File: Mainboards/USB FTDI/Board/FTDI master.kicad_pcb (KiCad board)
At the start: 2 copper layers, 67.4 x 54.3 mm, 52 parts, among them IC1 NCP1117ST, IC10 FT232RL, IC2 MCP1700T-1802E, IC3 CRE1S0505SC, IC4 IL0512S, IC5 IRF7416, IC7 MAX14932, IC8 MAX14932, IC9 MAX14932, J1 USB_C_Receptacle_USB2.0, X2 AKL18X-04W, X3 IDC-Header_2x05_P2.54mm_Verti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, X4 ALLSERIALMASTERM

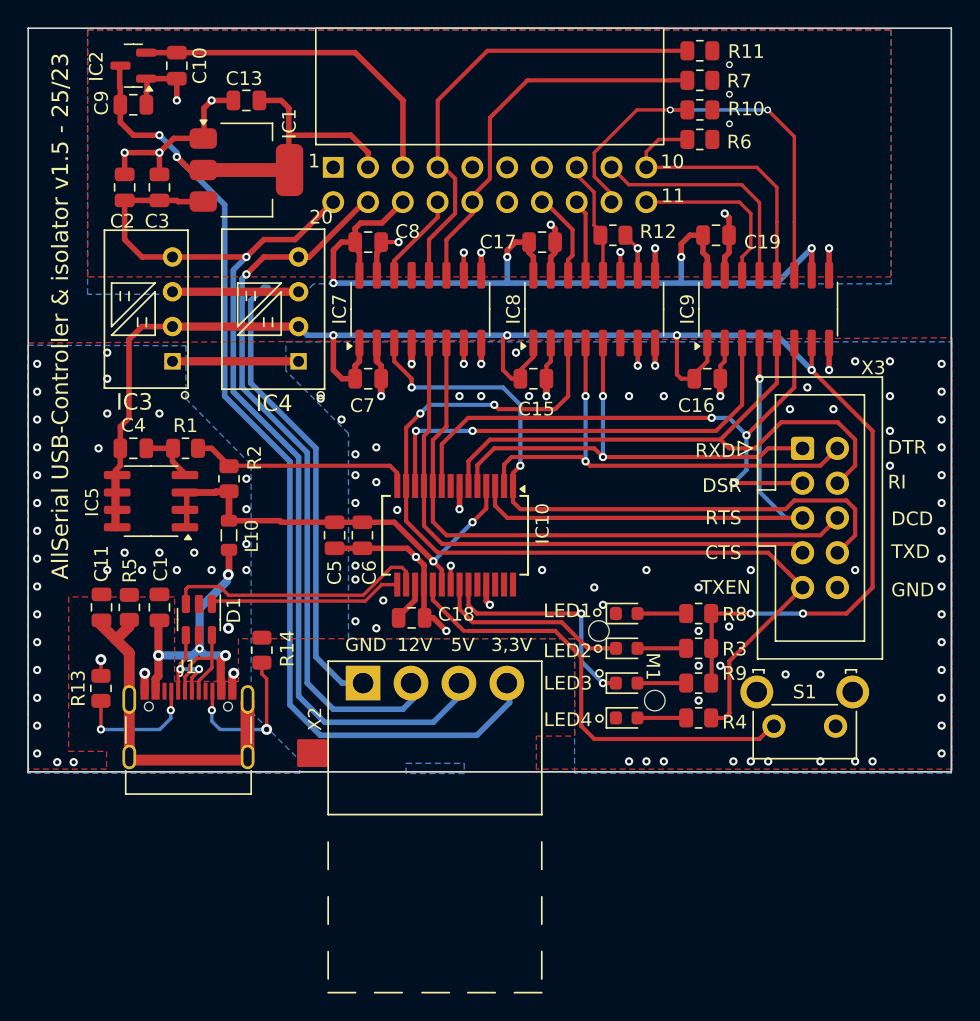
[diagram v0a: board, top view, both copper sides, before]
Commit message: Migrate to new KiCad Version
Add SMA connector front
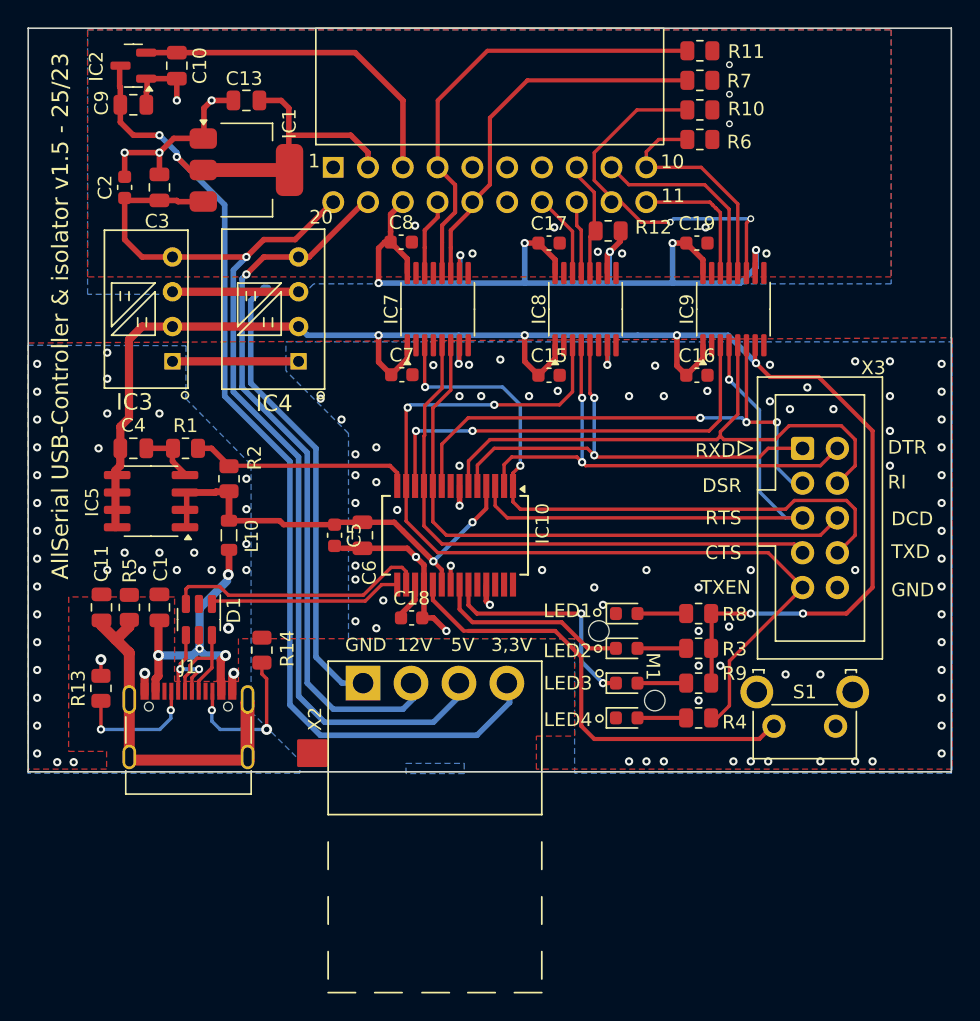
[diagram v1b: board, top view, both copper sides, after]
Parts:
- C15, C16, C17, C18, C19, C2, C5, C7, C8: footprint Capacitor_SMD:C_0805_2012Metric -> Capacitor_SMD:C_0603_1608Metric
- IC7, IC8, IC9: value MAX14932 -> ADuM142E0BRQZ-RL7; footprint Package_SO:SOIC-16_3.9x9.9mm_P1.27mm -> Package_SO:QSOP-16_3.9x4.9mm_P0.635mm
- L10: value WE-CBF_0805 -> ~
- moved IC9 2.54 mm to (166.3, 98.1)
- moved C7 2.48 mm to (142.1, 102.9)
- moved C8 2.41 mm to (142.0, 93.2)
- moved C19 1.51 mm to (163.6, 93.3)
- moved IC7 1.27 mm to (144.7, 98.1)
- moved C15 1.17 mm to (152.8, 102.9)
- moved C16 0.80 mm to (163.6, 102.9)
- moved IC8 0.64 mm to (155.5, 98.1)
- moved C17 0.51 mm to (152.8, 93.3)
- moved R12 0.47 mm to (157.1, 92.4)
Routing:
- net GND1: track 82.5 -> 62.9 mm
- net GND: track 48.2 -> 30.0 mm, vias 114 -> 115
- net Vio: track 74.1 -> 63.0 mm
- net Net-(IC9E-INB): track 32.1 -> 27.2 mm
- net +5V: track 131.6 -> 127.2 mm
- net Net-(IC10-~{DSR}): track 43.6 -> 39.7 mm
- net Net-(IC9D-INB): track 20.9 -> 17.3 mm
- net Net-(IC9C-OUTB): track 17.1 -> 14.5 mm
- net Net-(IC9B-OUTB): track 12.6 -> 10.1 mm
- net Net-(IC10-~{RI}): track 44.6 -> 42.6 mm
- net Net-(IC10-TXD): track 48.8 -> 47.3 mm
- net Net-(IC7B-OUTB): track 6.97 -> 6.01 mm
- net Net-(IC10-CBUS4): track 33.0 -> 32.1 mm
- net Net-(IC10-~{RTS}): track 39.0 -> 39.9 mm

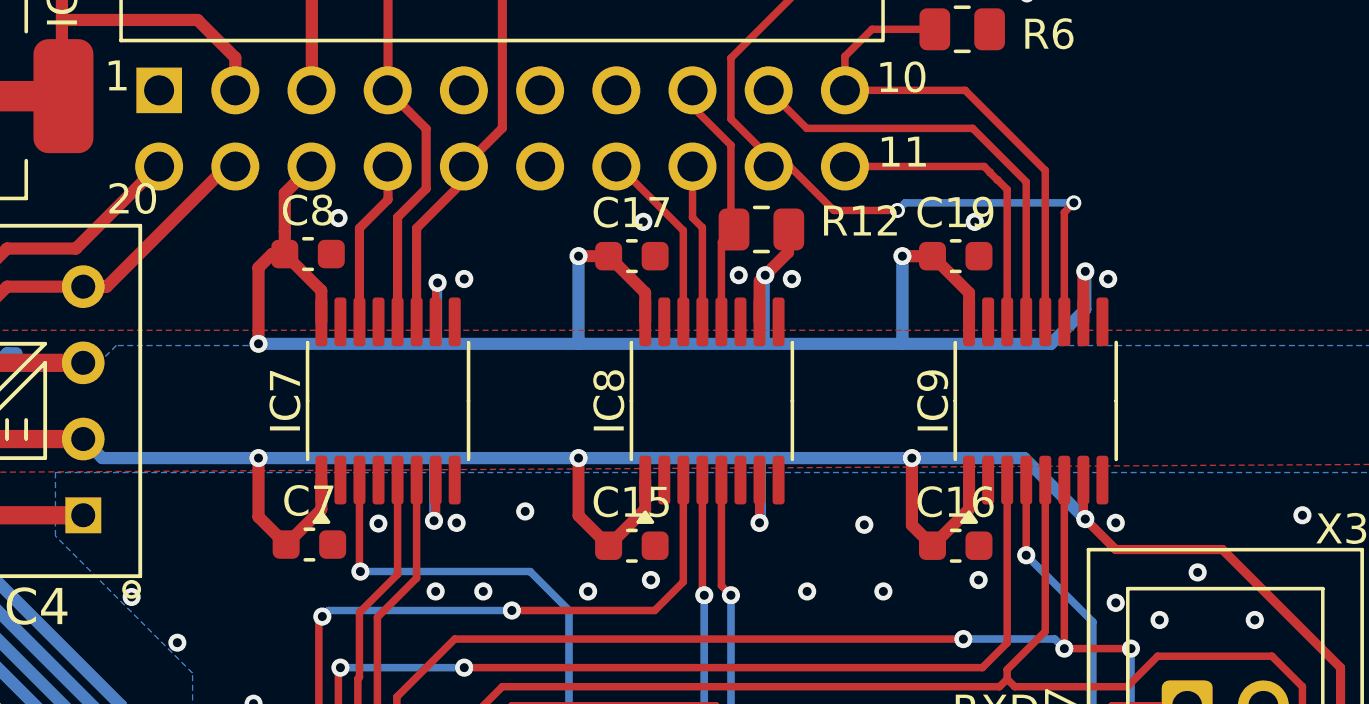
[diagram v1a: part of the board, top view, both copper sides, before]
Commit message: Update TTY CL slave board
Add ESP32 S3 WiFi MasterBoard
Update libs
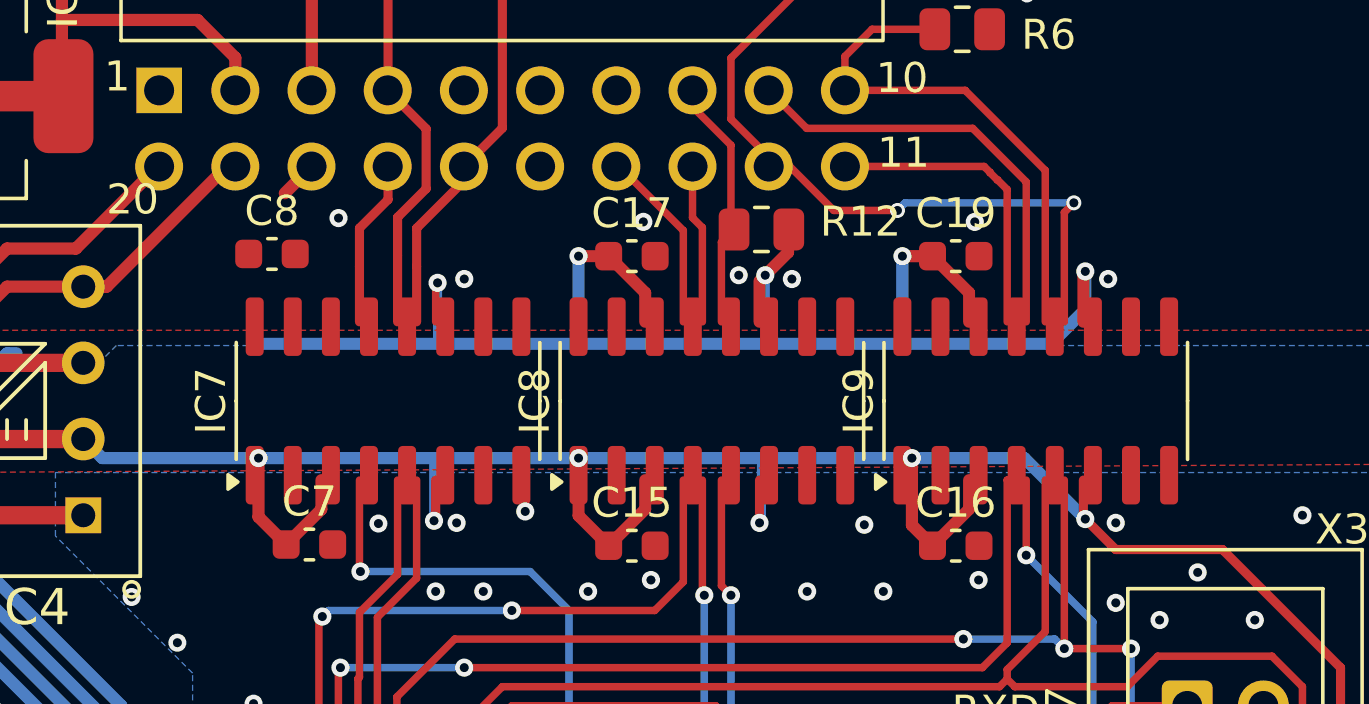
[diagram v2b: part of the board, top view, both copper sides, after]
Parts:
- IC7, IC8, IC9: footprint Package_SO:QSOP-16_3.9x4.9mm_P0.635mm -> Package_SO:SOIC-16_3.9x9.9mm_P1.27mm
- moved C8 1.20 mm to (140.8, 93.2)
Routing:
- net Vio: track 63.0 -> 54.6 mm, vias 6 -> 5

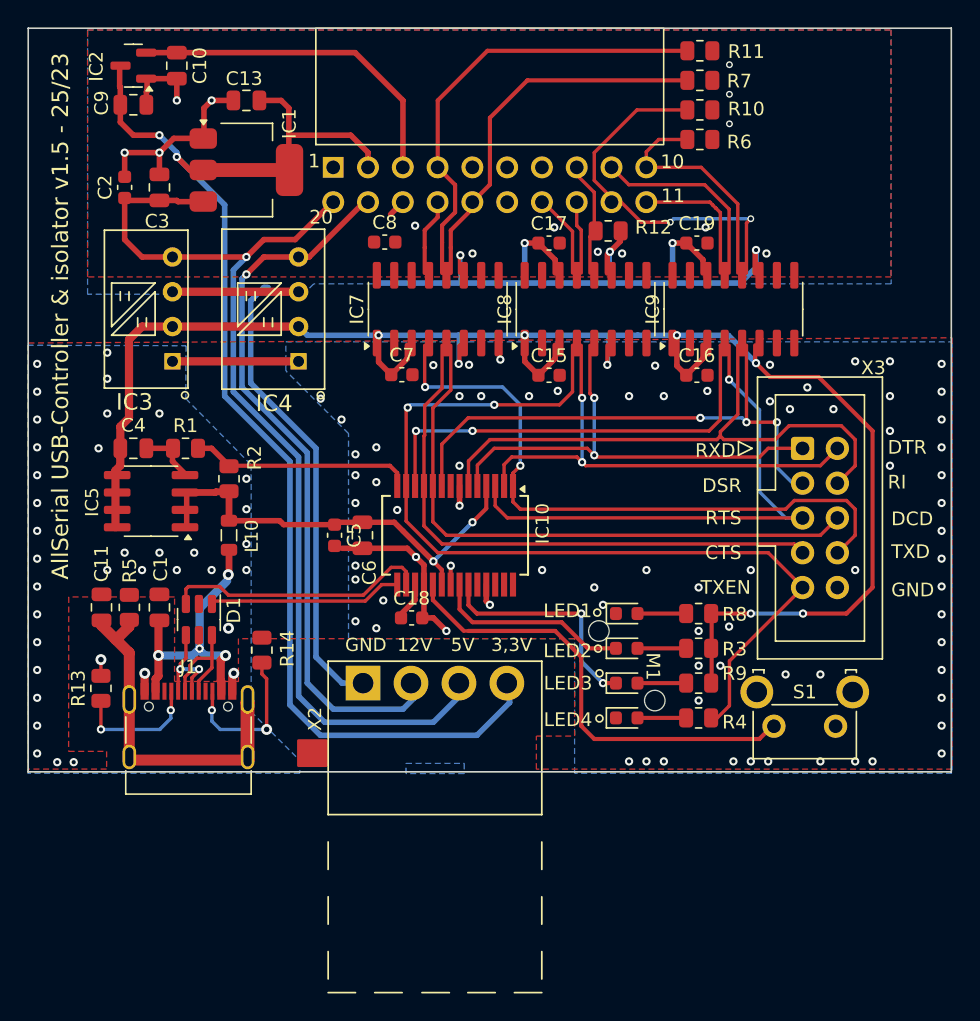
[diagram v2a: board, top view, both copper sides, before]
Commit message: Update AllSerial libraries
update projects
add slave project template
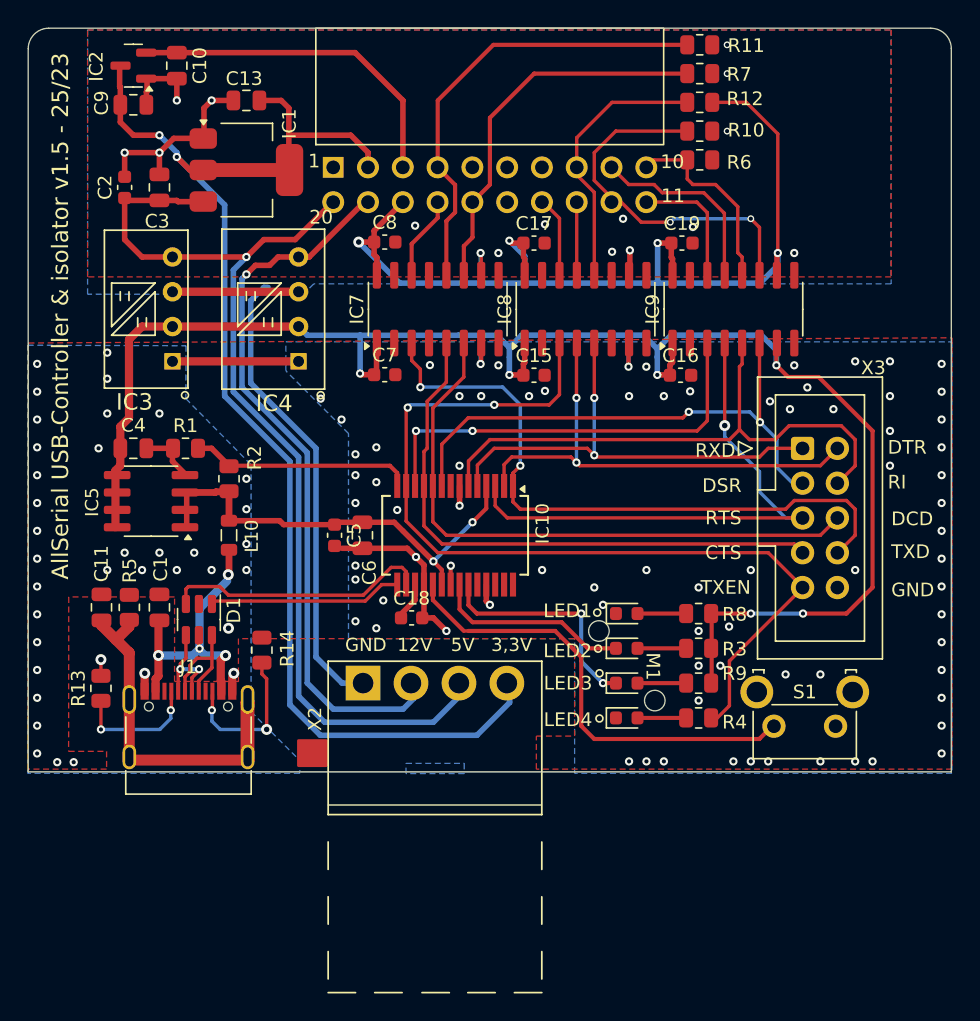
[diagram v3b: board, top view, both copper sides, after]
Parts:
- moved R12 11.5 mm to (163.8, 83.0)
- moved R10 1.55 mm to (163.8, 85.1)
- moved R6 1.49 mm to (163.8, 87.2)
- moved C7 1.25 mm to (140.8, 102.9)
- moved C16 1.19 mm to (162.4, 102.9)
- moved C15 1.10 mm to (151.7, 102.9)
- moved C17 1.10 mm to (151.7, 93.3)
- moved C19 1.09 mm to (162.5, 93.3)
- moved R7 0.49 mm to (163.8, 80.9)
- moved R11 0.43 mm to (163.8, 78.8)
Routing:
- net Vio: track 54.6 -> 79.6 mm, vias 5 -> 6
- net /RXDB: track 8.80 -> 19.7 mm
- net +5V: track 127.2 -> 131.2 mm
- net Net-(IC9D-INB): track 17.3 -> 14.3 mm
- net Net-(IC10-CBUS4): track 32.1 -> 31.3 mm
- net Net-(IC9B-OUTB): track 10.1 -> 9.35 mm
- net Net-(IC10-TXD): track 47.3 -> 48.1 mm
- net /TXENA: track 67.8 -> 67.1 mm
- net Net-(IC10-~{DCD}): track 43.9 -> 44.5 mm
- net Net-(IC7B-OUTB): track 6.01 -> 6.57 mm
- net Net-(IC10-~{DSR}): track 39.7 -> 39.5 mm, vias 3 -> 2
- net GND: track 30.0 -> 29.9 mm, vias 115 -> 114
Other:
- outline, holes or cut-outs redrawn

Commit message: improve board/front links
clean up
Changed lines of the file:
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@@
 		(pad_to_mask_clearance 0)
 		(allow_soldermask_bridges_in_footprints no)
-		(grid_origin 143.4211 98.1136)
+		(grid_origin 148.49 131.9)
 		(pcbplotparams
 			(layerselection 0x00010fc_ffffffff)
@@
 	)
 	(gr_rect
-		(start 134.52 129.614)
-		(end 136.552 131.446)
+		(start 134.52 130.514)
+		(end 136.452 131.646)
 		(stroke
 			(width 0.2)
@@
 	)
 	(via
-		(at 168.8211 131.1336)
+		(at 170.29 131.1336)
 		(size 0.6048)
 		(drill 0.3)
@@
 	)
 	(via
-		(at 166.2811 131.1336)
+		(at 164.49 131.1336)
 		(size 0.6048)
 		(drill 0.3)
@@
 	)
 	(via
-		(at 158.6611 131.1336)
+		(at 156.99 131.1336)
 		(size 0.6048)
 		(drill 0.3)
@@
 	)
 	(via
-		(at 118.11 131.191)
+		(at 119.99 131.2)
 		(size 0.6048)
 		(drill 0.3)
@@
 	)
 	(via
-		(at 167.5511 131.1336)
+		(at 166.79 131.1336)
 		(size 0.6048)
 		(drill 0.3)
@@
 	)
 	(via
-		(at 159.9311 131.1336)
+		(at 159.99 131.1336)
 		(size 0.6048)
 		(drill 0.3)
@@
 	)
 	(via
-		(at 175.1711 131.1336)
+		(at 174.49 131.1336)
 		(size 0.6048)
 		(drill 0.3)
@@
 		(polygon
 			(pts
-				(xy 146.6281 132.0226) (xy 142.3741 132.0226) (xy 142.3741 131.2766) (xy 146.6281 131.2766)
+				(xy 149.5281 131.9) (xy 147.4741 131.9) (xy 147.4741 131.154) (xy 149.5281 131.154)
 			)
 		)
@@
 		(polygon
 			(pts
-				(xy 161.544 131.953) (xy 157.988 131.953) (xy 157.988 130.683) (xy 161.544 130.683)
+				(xy 159.544 131.87) (xy 157.588 131.87) (xy 157.588 130.6) (xy 159.544 130.6)
 			)
 		)
@@
 		(polygon
 			(pts
-				(xy 173.99 131.953) (xy 169.926 131.953) (xy 169.926 130.683) (xy 173.99 130.683)
+				(xy 169.49 131.87) (xy 167.526 131.87) (xy 167.526 130.6) (xy 169.49 130.6)
 			)
 		)
@@
 		(polygon
 			(pts
-				(xy 146.812 131.953) (xy 142.24 131.953) (xy 142.24 131.064) (xy 146.812 131.064)
+				(xy 179.49 131.87) (xy 177.526 131.87) (xy 177.526 130.6) (xy 179.49 130.6)
 			)
 		)
@@
 		(polygon
 			(pts
-				(xy 135.763 131.953) (xy 132.842 131.953) (xy 132.842 130.683) (xy 135.763 130.683)
+				(xy 149.512 131.953) (xy 147.44 131.953) (xy 147.44 131.064) (xy 149.512 131.064)
 			)
 		)
@@
 		(polygon
 			(pts
-				(xy 118.872 131.953) (xy 116.332 131.953) (xy 116.332 130.556) (xy 118.872 130.556)
+				(xy 129.463 131.953) (xy 127.442 131.953) (xy 127.442 130.683) (xy 129.463 130.683)
+			)
+		)
+	)
+	(zone
+		(net 0)
+		(net_name "")
+		(layer "B.Mask")
+		(hatch edge 0.508)
+		(connect_pads
+			(clearance 0.000001)
+		)
+		(min_thickness 0.254)
+		(filled_areas_thickness no)
+		(fill yes
+			(thermal_gap 0.508)
+			(thermal_bridge_width 0.508)
+		)
+		(polygon
+			(pts
+				(xy 119.472 131.953) (xy 117.432 131.953) (xy 117.432 130.556) (xy 119.472 130.556)
 			)
 		)
@@
 		(polygon
 			(pts
-				(xy 176.53 131.953) (xy 173.99 131.953) (xy 173.99 130.302) (xy 176.53 130.302)
+				(xy 179.73 131.953) (xy 177.19 131.953) (xy 177.19 130.402) (xy 179.73 130.402)
 			)
 		)
@@
 		(polygon
 			(pts
-				(xy 168.91 131.953) (xy 166.37 131.953) (xy 166.37 130.302) (xy 168.91 130.302)
+				(xy 169.81 131.953) (xy 167.27 131.953) (xy 167.27 130.402) (xy 169.81 130.402)
 			)
 		)
@@
 		(polygon
 			(pts
-				(xy 136.482 131.572) (xy 134.442 131.572) (xy 134.442 129.667) (xy 136.482 129.667)
+				(xy 136.482 131.9) (xy 134.442 131.9) (xy 134.442 130.395) (xy 136.482 130.395)
 			)
 		)
@@
 		(polygon
 			(pts
-				(xy 120.538 131.953) (xy 119.014 131.953) (xy 119.014 130.429) (xy 120.538 130.429)
+				(xy 119.238 131.953) (xy 117.714 131.953) (xy 117.714 130.429) (xy 119.238 130.429)
 			)
 		)
@@
 		(polygon
 			(pts
-				(xy 154.94 131.572) (xy 152.654 131.572) (xy 152.654 129.286) (xy 154.94 129.286)
+				(xy 154.84 131.872) (xy 152.754 131.872) (xy 152.754 130.386) (xy 154.84 130.386)
 			)
 		)
@@
 		(min_thickness 0.254)
 		(filled_areas_thickness no)
-		(fill yes
+		(fill
 			(thermal_gap 0.508)
 			(thermal_bridge_width 0.508)
@@
 		(polygon
 			(pts
-				(xy 182.245 132.715) (xy 180.975 132.715) (xy 180.975 100.33) (xy 182.245 100.33)
+				(xy 182.245 132.015) (xy 180.975 132.015) (xy 180.975 100.33) (xy 182.245 100.33)
 			)
 		)
@@
 		(min_thickness 0.254)
 		(filled_areas_thickness no)
-		(fill yes
+		(fill
 			(thermal_gap 0.508)
 			(thermal_bridge_width 0.508)
@@
 		(polygon
 			(pts
-				(xy 115.824 132.08) (xy 114.3 132.08) (xy 114.3 100.584) (xy 115.824 100.6475)
+				(xy 115.824 132.08) (xy 114.3 132.08) (xy 114.3 100.6) (xy 115.824 100.6)
 			)
 		)
